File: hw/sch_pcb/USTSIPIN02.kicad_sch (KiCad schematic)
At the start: 5 parts, among them M1 HOLE, M2 HOLE, M3 HOLE, M4 HOLE, M8 BMI-S-204-F

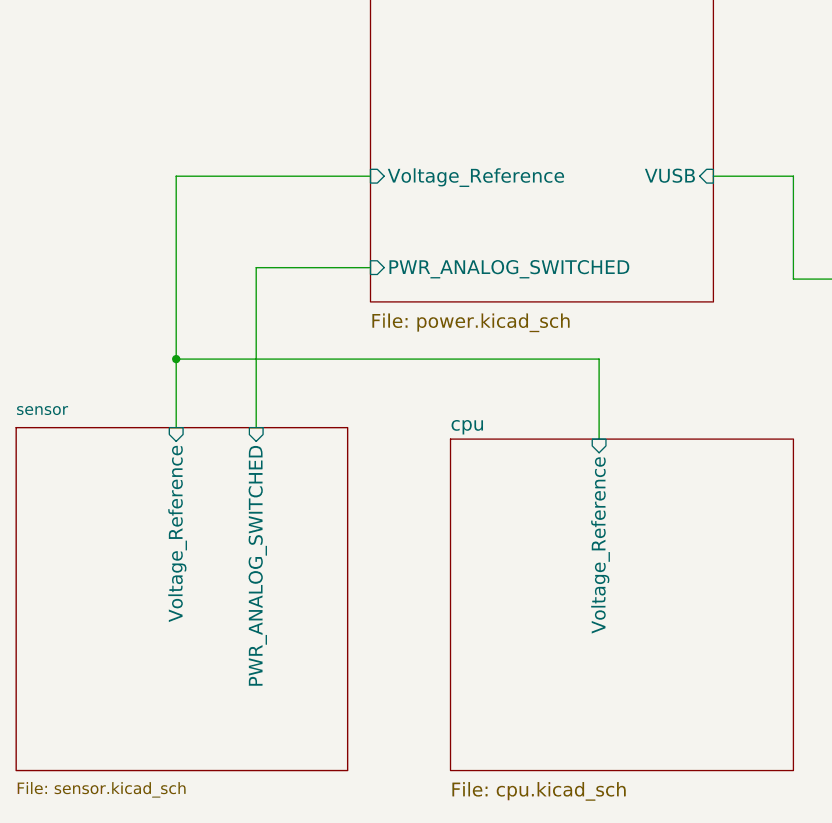
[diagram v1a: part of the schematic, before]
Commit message: Changed virtual ground to programmable reference. Add test points Primary power filters changed to LC.
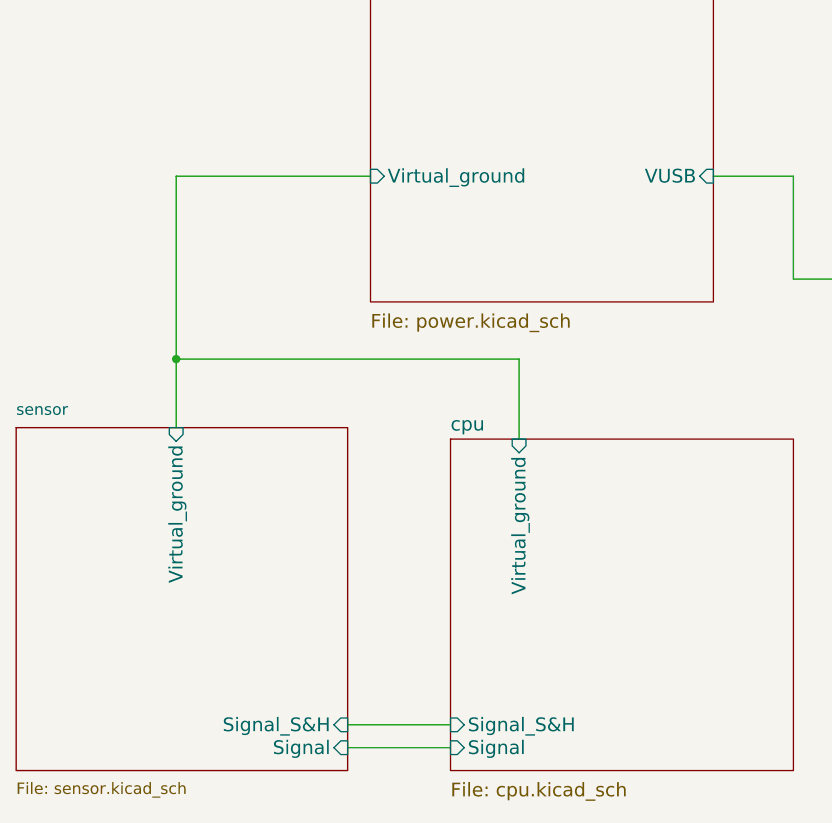
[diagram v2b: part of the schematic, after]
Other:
- sheet cpu ports: added Signal, Signal_S&H, Virtual_ground; removed Voltage_Reference
- sheet power ports: added Virtual_ground; removed PWR_ANALOG_SWITCHED, Voltage_Reference
- sheet sensor ports: added Signal, Signal_S&H, Virtual_ground; removed PWR_ANALOG_SWITCHED, Voltage_Reference
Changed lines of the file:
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@@
     (stroke (width 0) (type default))
   )
-  (wire (pts (xy 72.39 72.39) (xy 85.09 72.39))
-    (stroke (width 0) (type default))
-  )
-  (wire (pts (xy 110.49 82.55) (xy 63.5 82.55))
+  (wire (pts (xy 101.6 82.55) (xy 63.5 82.55))
     (stroke (width 0) (type default))
   )
@@
     (stroke (width 0) (type solid))
   )
-  (wire (pts (xy 72.39 90.17) (xy 72.39 72.39))
-    (stroke (width 0) (type default))
-  )
   (wire (pts (xy 262.89 17.78) (xy 262.89 16.51))
     (stroke (width 0) (type solid))
   )
+  (wire (pts (xy 82.55 123.19) (xy 93.98 123.19))
+    (stroke (width 0) (type default))
+  )
   (wire (pts (xy 273.05 17.78) (xy 273.05 16.51))
     (stroke (width 0) (type solid))
@@
     (stroke (width 0) (type solid))
   )
+  (wire (pts (xy 82.55 125.73) (xy 93.98 125.73))
+    (stroke (width 0) (type default))
+  )
   (wire (pts (xy 262.89 16.51) (xy 267.97 16.51))
     (stroke (width 0) (type solid))
   )
-  (wire (pts (xy 110.49 91.44) (xy 110.49 82.55))
+  (wire (pts (xy 101.6 91.44) (xy 101.6 82.55))
     (stroke (width 0) (type default))
   )
@@
       (effects (font (size 1.524 1.524)) (justify left top))
     )
-    (pin "Voltage_Reference" input (at 110.49 91.44 90)
-      (effects (font (size 1.524 1.524)) (justify right))
+    (pin "Virtual_ground" input (at 101.6 91.44 90)
+      (effects (font (size 1.524 1.524)) (justify right))
+    )
+    (pin "Signal" input (at 93.98 125.73 180)
+      (effects (font (size 1.524 1.524)) (justify left))
+    )
+    (pin "Signal_S&H" input (at 93.98 123.19 180)
+      (effects (font (size 1.524 1.524)) (justify left))
     )
     (instances
@@
       (effects (font (size 1.524 1.524)) (justify right))
     )
-    (pin "PWR_ANALOG_SWITCHED" input (at 85.09 72.39 180)
-      (effects (font (size 1.524 1.524)) (justify left))
-    )
-    (pin "Voltage_Reference" input (at 85.09 62.23 180)
+    (pin "Virtual_ground" input (at 85.09 62.23 180)
       (effects (font (size 1.524 1.524)) (justify left))
     )
@@
       (effects (font (size 1.27 1.27)) (justify left top))
     )
-    (pin "PWR_ANALOG_SWITCHED" input (at 72.39 90.17 90)
-      (effects (font (size 1.524 1.524)) (justify right))
-    )
-    (pin "Voltage_Reference" input (at 63.5 90.17 90)
-      (effects (font (size 1.524 1.524)) (justify right))
-    )
+    (pin "Virtual_ground" input (at 63.5 90.17 90)
+      (effects (font (size 1.524 1.524)) (justify right))
+    )
+    (pin "Signal_S&H" input (at 82.55 123.19 0)
+      (effects (font (size 1.524 1.524)) (justify right))
+    )
+    (pin "Signal" input (at 82.55 125.73 0)
+      (effects (font (size 1.524 1.524)) (justify right))
+    )

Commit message: PCB routing.
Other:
- sheet cpu ports: added SCL, SDA; removed none
- sheet sensor ports: added SCL, SDA; removed none
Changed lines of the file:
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@@
     (stroke (width 0) (type solid))
+  )
+  (wire (pts (xy 82.55 113.03) (xy 93.98 113.03))
+    (stroke (width 0) (type default))
   )
   (wire (pts (xy 123.19 62.23) (xy 132.08 62.23))
@@
   (wire (pts (xy 278.13 17.78) (xy 278.13 16.51))
     (stroke (width 0) (type solid))
+  )
+  (wire (pts (xy 82.55 115.57) (xy 93.98 115.57))
+    (stroke (width 0) (type default))
   )
   (wire (pts (xy 267.97 16.51) (xy 273.05 16.51))
@@
     )
     (pin "Signal_S&H" input (at 93.98 123.19 180)
+      (effects (font (size 1.524 1.524)) (justify left))
+    )
+    (pin "SCL" input (at 93.98 113.03 180)
+      (effects (font (size 1.524 1.524)) (justify left))
+    )
+    (pin "SDA" input (at 93.98 115.57 180)
       (effects (font (size 1.524 1.524)) (justify left))
     )
@@
       (effects (font (size 1.524 1.524)) (justify right))
     )
+    (pin "SCL" input (at 82.55 113.03 0)
+      (effects (font (size 1.524 1.524)) (justify right))
+    )
+    (pin "SDA" input (at 82.55 115.57 0)
+      (effects (font (size 1.524 1.524)) (justify right))
+    )

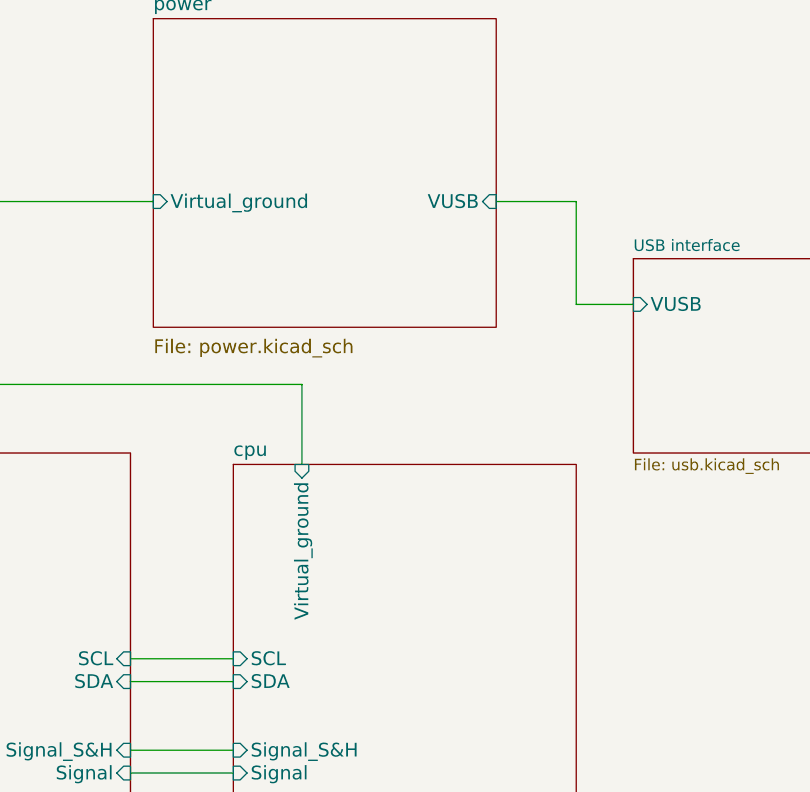
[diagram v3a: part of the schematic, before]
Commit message: change global reset label to page pins. aling schematics symbols to grid for MCU page.
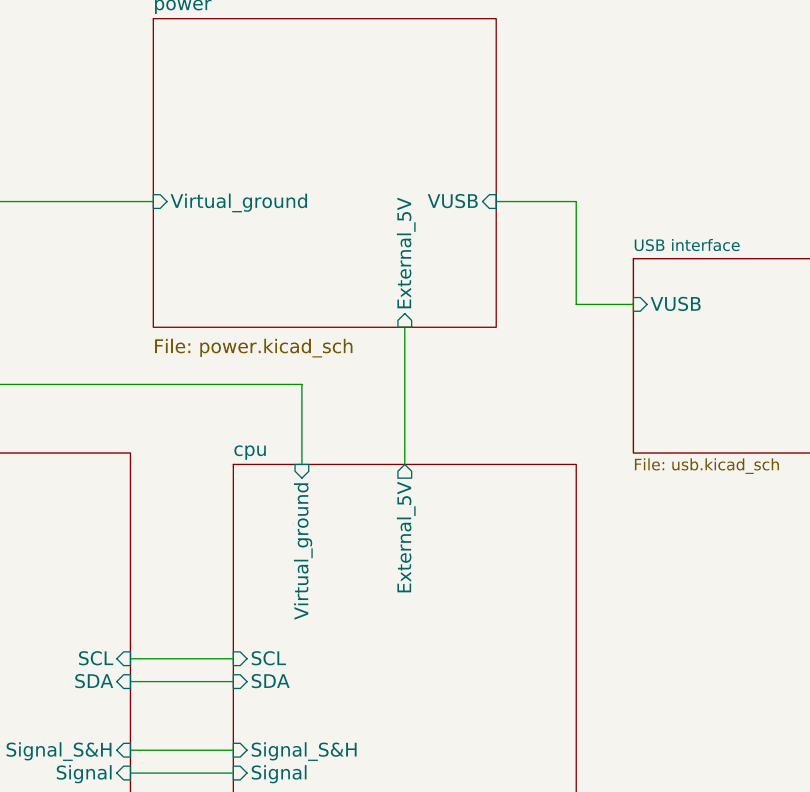
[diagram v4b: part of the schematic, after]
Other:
- sheet cpu ports: added External_5V; removed none
- sheet power ports: added External_5V; removed none
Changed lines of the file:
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@@
+    (stroke (width 0) (type default))
+  )
+  (wire (pts (xy 113.03 76.2) (xy 113.03 91.44))
     (stroke (width 0) (type default))
   )
@@
       (effects (font (size 1.524 1.524)) (justify left))
     )
+    (pin "External_5V" output (at 113.03 91.44 90)
+      (effects (font (size 1.524 1.524)) (justify right))
+    )
     (instances
       (project "USTSIPIN02"
@@
       (effects (font (size 1.524 1.524)) (justify left))
     )
+    (pin "External_5V" input (at 113.03 76.2 270)
+      (effects (font (size 1.524 1.524)) (justify left))
+    )

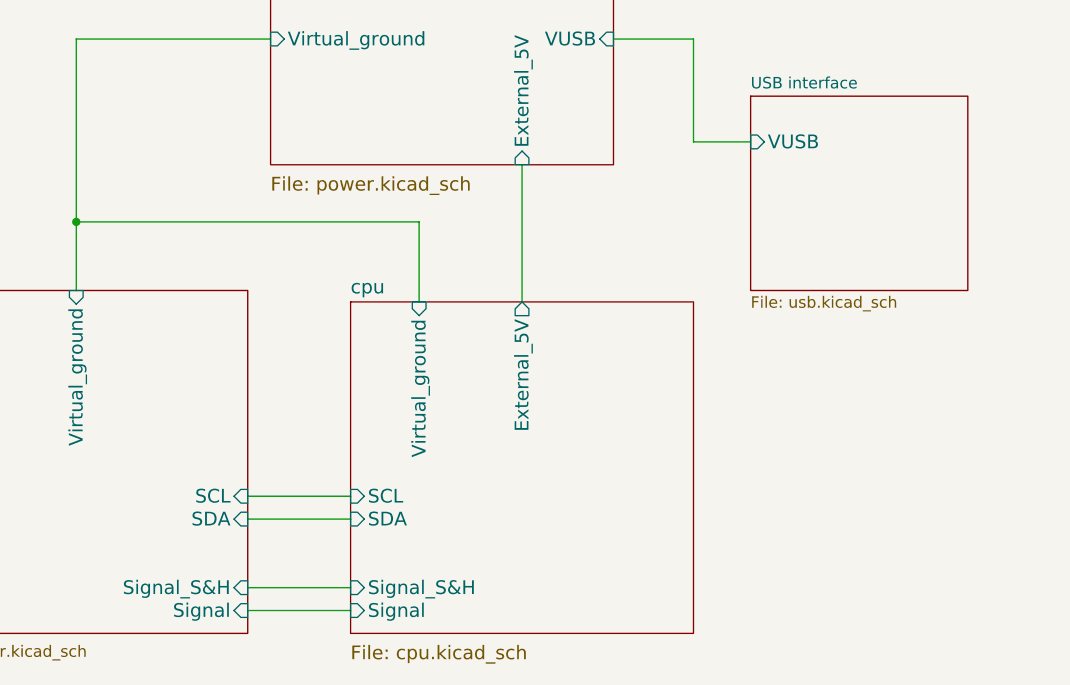
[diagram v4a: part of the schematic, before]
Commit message: Update schematics symbols Add protection  resistor to external connectors. Reorganising digital part of PCB.
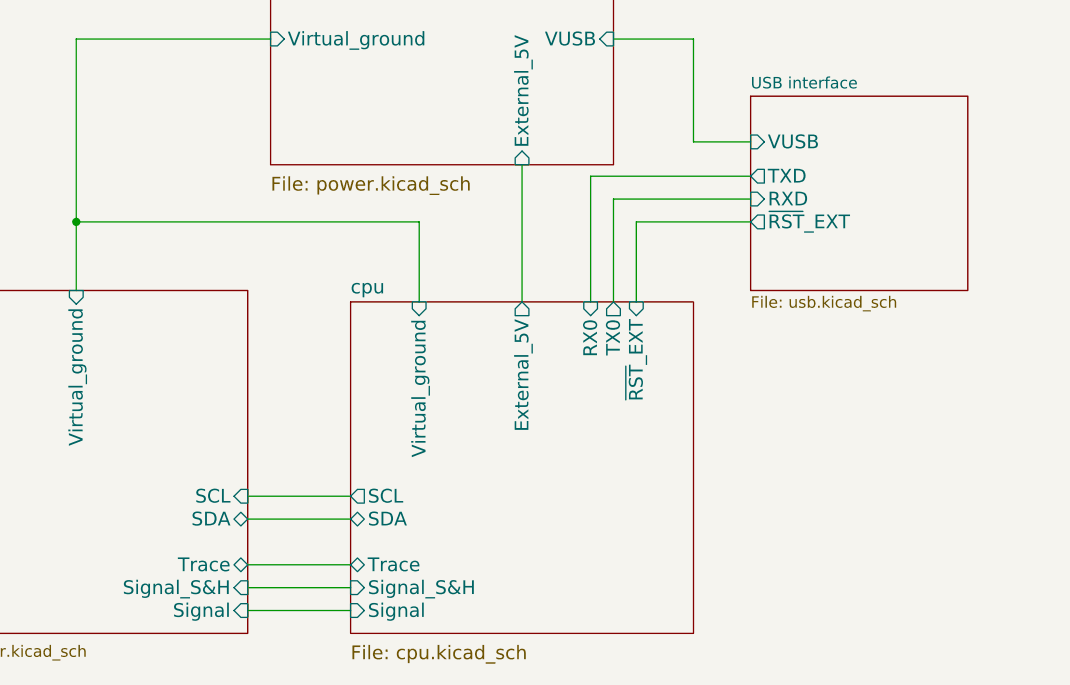
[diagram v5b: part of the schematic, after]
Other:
- sheet USB interface ports: added RXD, TXD, ~{RST}_EXT; removed none
- sheet cpu ports: added RX0, TX0, Trace, ~{RST}_EXT; removed none
- sheet sensor ports: added Trace; removed none
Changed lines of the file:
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@@
   (junction (at 267.97 16.51) (diameter 0) (color 0 0 0 0)
   )
+  (wire (pts (xy 82.55 120.65) (xy 93.98 120.65))
+    (stroke (width 0) (type default))
+  )
   (wire (pts (xy 63.5 90.17) (xy 63.5 82.55))
     (stroke (width 0) (type default))
@@
   )
   (wire (pts (xy 123.19 62.23) (xy 132.08 62.23))
+    (stroke (width 0) (type default))
+  )
+  (wire (pts (xy 138.43 82.55) (xy 125.73 82.55))
     (stroke (width 0) (type default))
   )
@@
     (stroke (width 0) (type dash))
   )
+  (wire (pts (xy 125.73 82.55) (xy 125.73 91.44))
+    (stroke (width 0) (type default))
+  )
   (wire (pts (xy 267.97 17.78) (xy 267.97 16.51))
     (stroke (width 0) (type solid))
@@
     (stroke (width 0) (type default))
   )
+  (wire (pts (xy 138.43 77.47) (xy 120.65 77.47))
+    (stroke (width 0) (type default))
+  )
   (wire (pts (xy 113.03 76.2) (xy 113.03 91.44))
     (stroke (width 0) (type default))
@@
     (stroke (width 0) (type solid))
   )
+  (wire (pts (xy 120.65 77.47) (xy 120.65 91.44))
+    (stroke (width 0) (type default))
+  )
+  (wire (pts (xy 123.19 80.01) (xy 123.19 91.44))
+    (stroke (width 0) (type default))
+  )
   (wire (pts (xy 82.55 123.19) (xy 93.98 123.19))
     (stroke (width 0) (type default))
@@
   (wire (pts (xy 273.05 17.78) (xy 273.05 16.51))
     (stroke (width 0) (type solid))
+  )
+  (wire (pts (xy 138.43 80.01) (xy 123.19 80.01))
+    (stroke (width 0) (type default))
   )
   (wire (pts (xy 132.08 73.66) (xy 138.43 73.66))
@@
       (effects (font (size 1.524 1.524)) (justify left))
     )
-    (pin "SCL" input (at 93.98 113.03 180)
-      (effects (font (size 1.524 1.524)) (justify left))
-    )
-    (pin "SDA" input (at 93.98 115.57 180)
+    (pin "SCL" output (at 93.98 113.03 180)
+      (effects (font (size 1.524 1.524)) (justify left))
+    )
+    (pin "SDA" bidirectional (at 93.98 115.57 180)
       (effects (font (size 1.524 1.524)) (justify left))
     )
     (pin "External_5V" output (at 113.03 91.44 90)
+      (effects (font (size 1.524 1.524)) (justify right))
+    )
+    (pin "~{RST}_EXT" input (at 125.73 91.44 90)
+      (effects (font (size 1.524 1.524)) (justify right))
+    )
+    (pin "Trace" bidirectional (at 93.98 120.65 180)
+      (effects (font (size 1.524 1.524)) (justify left))
+    )
+    (pin "TX0" output (at 123.19 91.44 90)
+      (effects (font (size 1.524 1.524)) (justify right))
+    )
+    (pin "RX0" input (at 120.65 91.44 90)
       (effects (font (size 1.524 1.524)) (justify right))
     )
@@
       (effects (font (size 1.524 1.524)) (justify left))
     )
+    (pin "~{RST}_EXT" output (at 138.43 82.55 180)
+      (effects (font (size 1.524 1.524)) (justify left))
+    )
+    (pin "TXD" output (at 138.43 77.47 180)
+      (effects (font (size 1.524 1.524)) (justify left))
+    )
+    (pin "RXD" input (at 138.43 80.01 180)
+      (effects (font (size 1.524 1.524)) (justify left))
+    )
     (instances
       (project "USTSIPIN02"
@@
       (effects (font (size 1.524 1.524)) (justify right))
     )
-    (pin "SDA" input (at 82.55 115.57 0)
-      (effects (font (size 1.524 1.524)) (justify right))
-    )
+    (pin "SDA" bidirectional (at 82.55 115.57 0)
+      (effects (font (size 1.524 1.524)) (justify right))
+    )
+    (pin "Trace" bidirectional (at 82.55 120.65 0)
+      (effects (font (size 1.524 1.524)) (justify right))
+    )
